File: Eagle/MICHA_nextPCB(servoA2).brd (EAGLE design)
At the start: 110.5 x 83.1 mm, 71 parts, among them IC1 LM4041A12LP, K1 PIN20X2, T1 BSS84, U1 ARDUINO_MKR_ZERO, U2 MIKROE_CLICK_UPGRADE, U3 MAX4528CSA, X1 SS-7188S-A-NF_V2, X2 SS-7188S-A-NF_V2, X3 SS-7188S-A-NF_V2, X4 SS-7188S-A-NF_V2, X5 SS-7188S-A-NF_V2, X6 SS-7188S-A-NF_V2, X7 BUCHANAN_4_3.5MM, X8 MPT_0,5/_2-2,54_1725656_2

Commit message: Btn & thermis zener replaced by Schottky
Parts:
- removed Z10, Z4, Z5, Z6, Z7, Z8, Z9: 3,3V, Zener_SMA:ZENER_SMA
- added DS1, DS2, DS3, DS4: SDM10M45SD, SchottkyDiodes_SDM10M45SD:SDM10M45SD_SOT-26
- moved R21 3.17 mm to (21.0, -0.64)
- moved R14 2.22 mm to (19.4, 8.57)
- moved R15 2.22 mm to (22.5, 8.57)
- moved R16 2.22 mm to (25.7, 8.57)
- moved R13 0.95 mm to (16.2, 8.57)
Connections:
- net GND: now also DS1.1, DS1.4, DS2.1, DS2.4, DS3.1, DS3.4, DS4.1, DS4.4; no longer Z10.A, Z4.A, Z5.A, Z6.A, Z7.A, Z8.A, Z9.A
- net N$11: now also DS1.3; no longer Z4.C
- net N$12: now also DS1.6; no longer Z5.C
- net N$13: now also DS2.3; no longer Z6.C
- net N$14: now also DS2.6; no longer Z7.C
- net PI_STOP_BTN: now also DS4.3; no longer Z10.C
- net PUMP_PAUSE_BTN: now also DS3.6; no longer Z8.C
- net PUMP_START_BTN: now also DS3.3; no longer Z9.C
- net VDD: now also DS1.2, DS1.5, DS2.2, DS2.5, DS3.2, DS3.5, DS4.2, DS4.5
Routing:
- net VDD: track 51.5 -> 168.6 mm, vias 1 -> 9
- net N$11: track 85.0 -> 75.9 mm
- net N$14: track 63.4 -> 72.3 mm
- net N$13: track 74.8 -> 69.6 mm
- net N$6: track 87.4 -> 84.7 mm
- net N$12: track 72.6 -> 74.6 mm
- net GND: track 8.64 -> 10.6 mm, vias 4 -> 6
- net THERMI2: track 6.82 -> 5.51 mm
- net PUMP_START_BTN: track 66.3 -> 65.4 mm

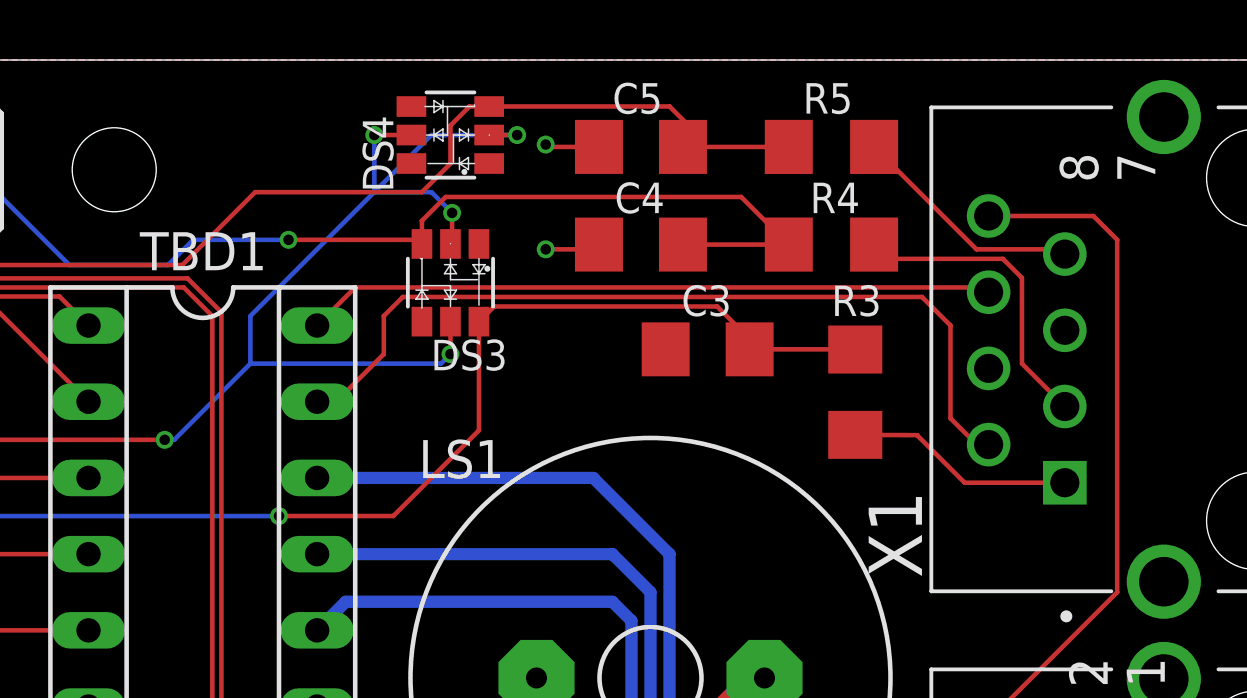
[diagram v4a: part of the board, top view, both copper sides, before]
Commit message: Button diodes between resistor and capacitor
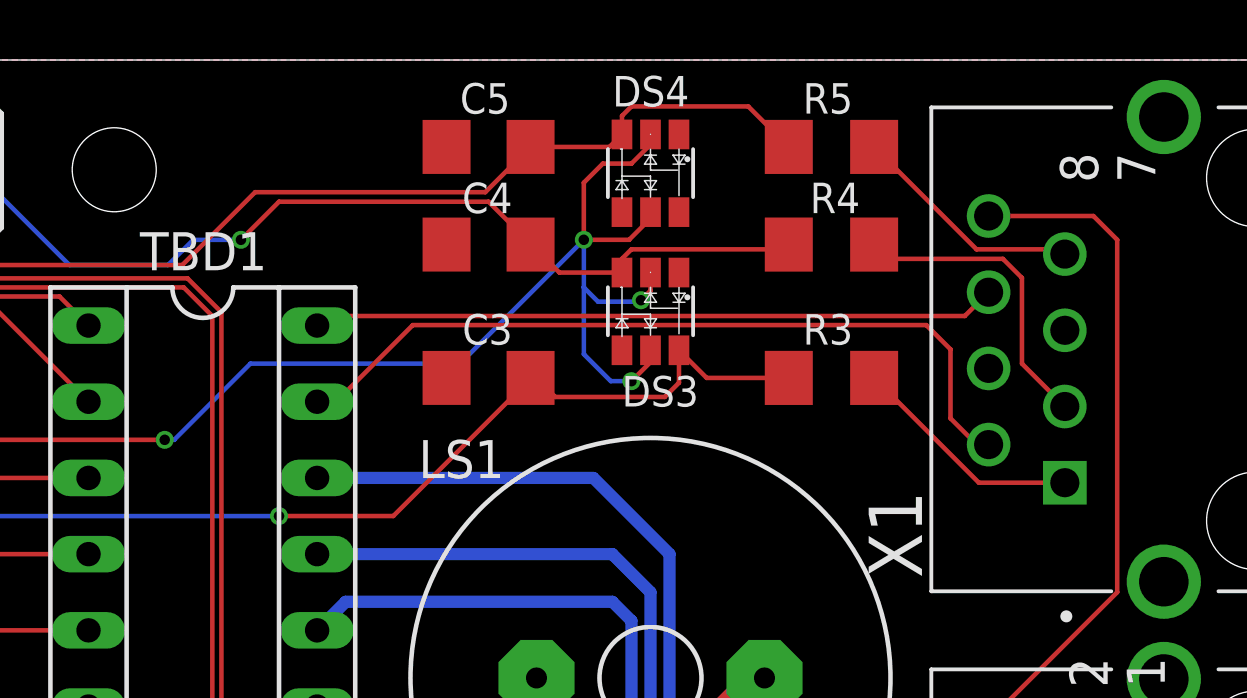
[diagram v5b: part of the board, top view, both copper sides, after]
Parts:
- moved C3 7.36 mm to (74.0, 45.6)
- moved DS4 6.79 mm to (79.4, 52.4), turned to 180 degrees
- moved DS3 6.74 mm to (79.4, 47.8)
- moved C4 5.08 mm to (74.0, 50.0)
- moved C5 5.08 mm to (74.0, 53.3)
- moved R3 0.93 mm to (85.4, 45.6), turned to 0 degrees
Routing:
- net PUMP_PAUSE_BTN: track 72.8 -> 68.6 mm
- net GND: track 10.6 -> 6.98 mm, vias 6 -> 4
- net PUMP_START_BTN: track 65.4 -> 62.3 mm
- net PUMP_PAUSE_LED: track 28.4 -> 26.4 mm
- net VDD: track 168.6 -> 170.5 mm, vias 9 -> 8
- net PI_STOP_BTN: track 40.0 -> 39.1 mm

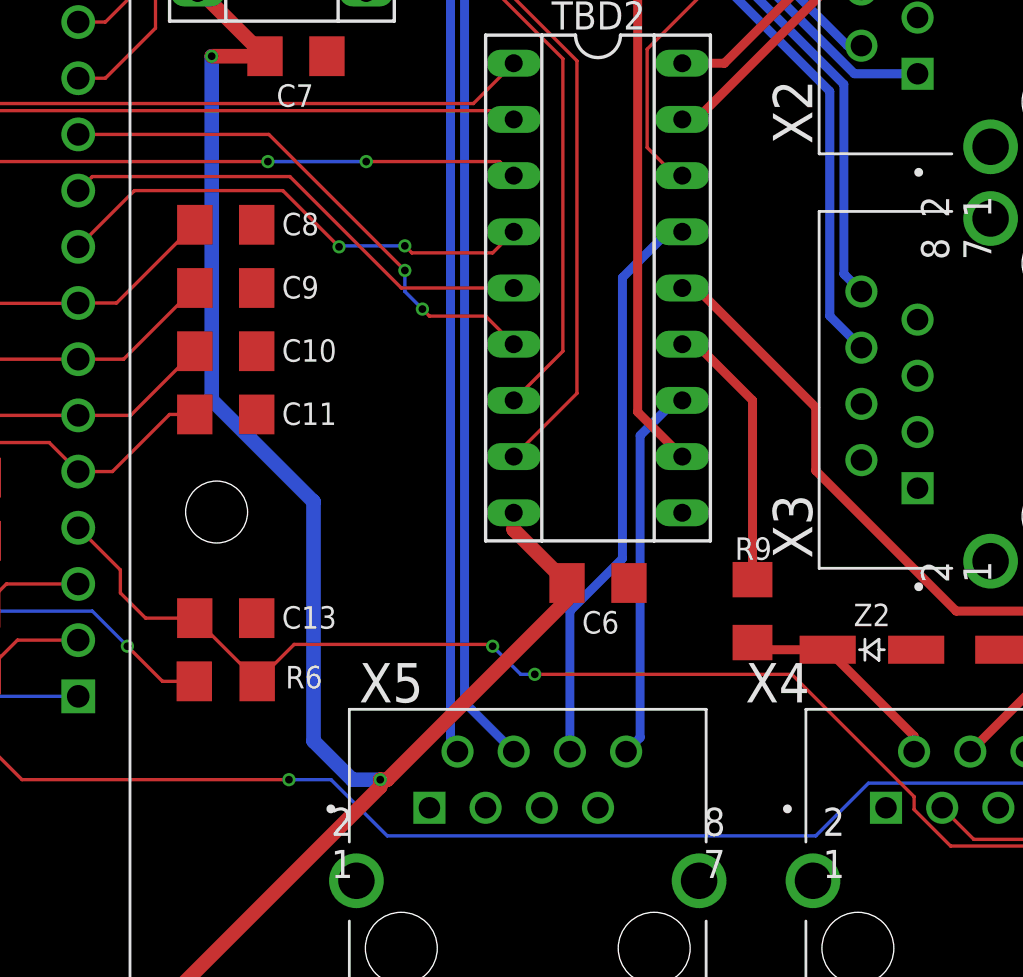
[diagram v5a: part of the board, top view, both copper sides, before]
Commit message: add jumpers for reserve and pump_relay
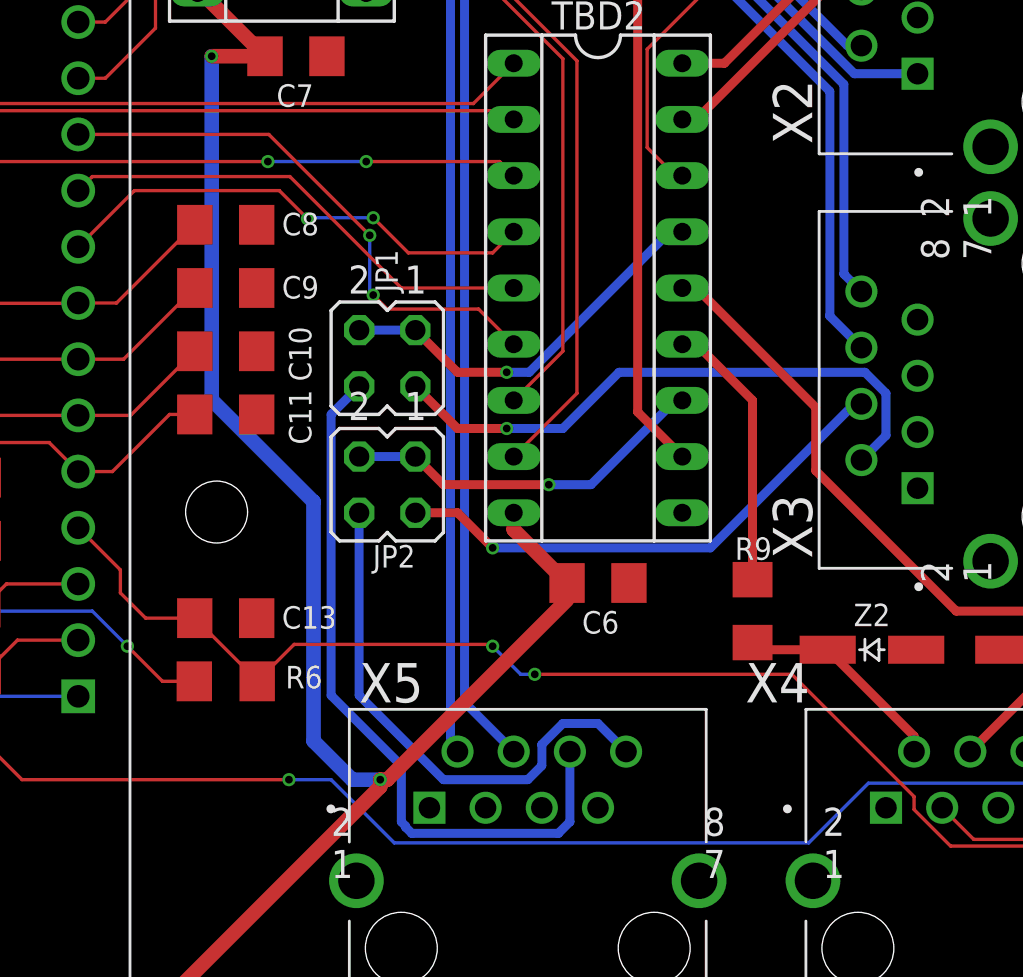
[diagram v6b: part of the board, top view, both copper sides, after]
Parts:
- added JP1, JP2: (no value), jumper:JP2Q
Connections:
- new net N$19: JP1.4, X5.6
- new net N$20: JP1.2, X3.2
- new net N$21: JP2.4, X5.8
- new net N$22: JP2.2, X3.4
- net PUMP_RELAY: now also JP1.1, JP1.3; no longer X5.6
- net RESERVE: now also JP2.1, JP2.3; no longer X5.8
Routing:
- net N$19: track 0.00 -> 32.8 mm
- net N$20: track 0.00 -> 27.0 mm, vias 0 -> 1
- net N$21: track 0.00 -> 24.0 mm
- net N$22: track 0.00 -> 23.5 mm, vias 0 -> 1
- net PUMP_RELAY: track 26.0 -> 18.0 mm, vias 0 -> 1
- net D2: track 24.2 -> 25.2 mm
- net RESERVE: track 17.1 -> 16.7 mm, vias 0 -> 1

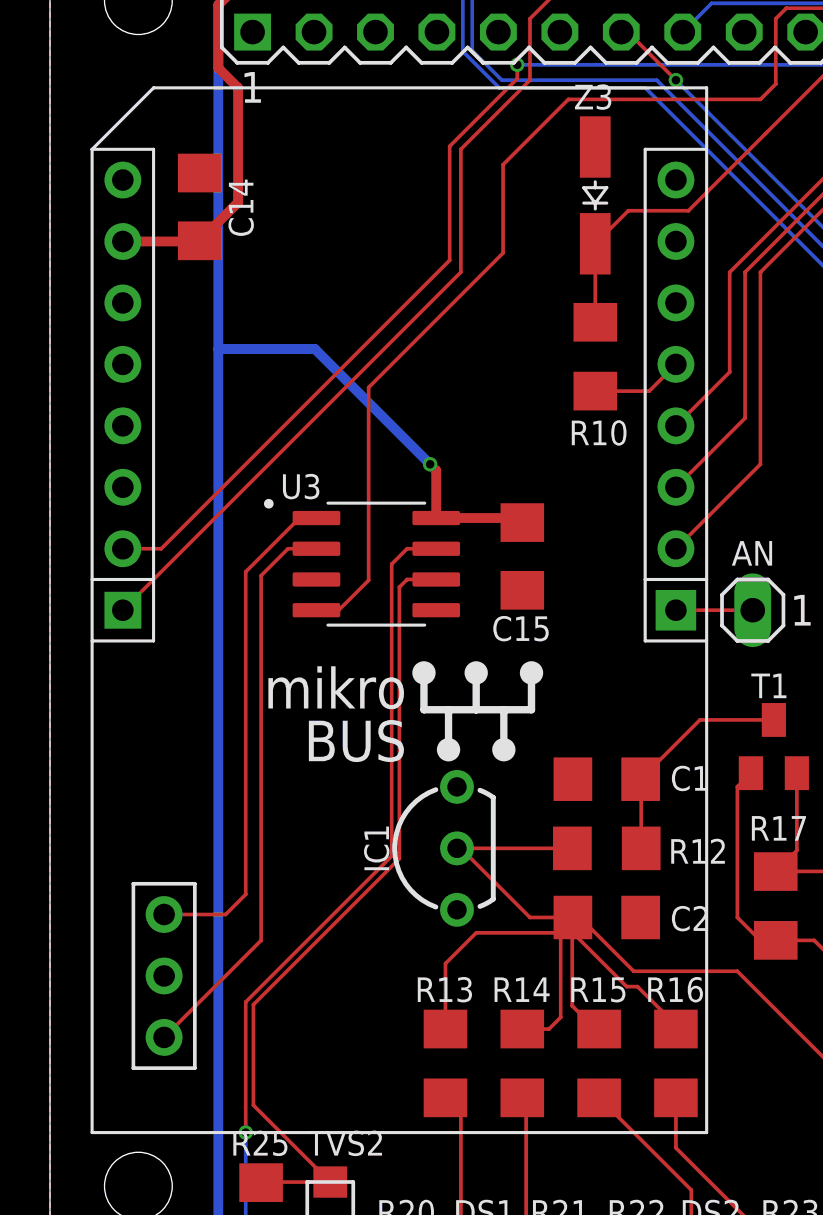
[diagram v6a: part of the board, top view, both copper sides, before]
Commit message: Mikrobus footprint updated
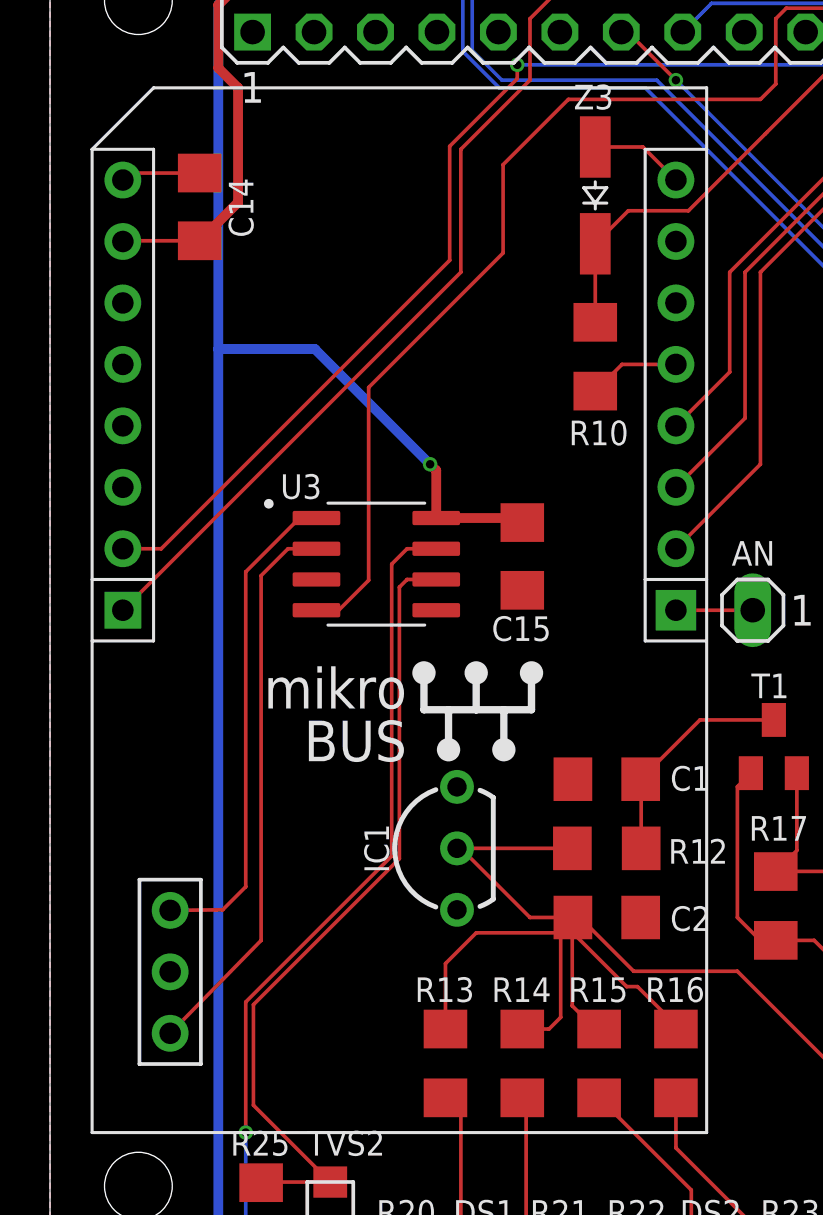
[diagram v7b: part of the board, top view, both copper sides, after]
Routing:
- net GND: track 6.98 -> 14.2 mm
- net N$10: track 20.9 -> 20.4 mm
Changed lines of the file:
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@@
 <contactref element="C13" pad="2"/>
 <contactref element="C14" pad="2"/>
-<contactref element="U2" pad="R_GND2"/>
-<contactref element="U2" pad="R_GND1"/>
 <contactref element="Z1" pad="A"/>
 <contactref element="Z2" pad="A"/>
@@
 <contactref element="DS4" pad="1"/>
 <contactref element="DS4" pad="4"/>
+<contactref element="U2" pad="R_GND1"/>
+<contactref element="U2" pad="R_GND2"/>
+<wire x1="25.7175" y1="45.085" x2="24.3525" y2="46.45" width="0.1524" layer="1"/>
+<wire x1="24.3525" y1="46.45" x2="22.38375" y2="46.45" width="0.1524" layer="1"/>
+<wire x1="2.8575" y1="45.085" x2="3.14625" y2="45.37375" width="0.1524" layer="1"/>
+<wire x1="3.14625" y1="45.37375" x2="6.0325" y2="45.37375" width="0.1524" layer="1"/>
 </signal>
 <signal name="5V">
@@
 <wire x1="15.5575" y1="33.3375" x2="10.795" y2="38.1" width="0.4064" layer="16"/>
 <wire x1="10.795" y1="38.1" x2="6.8032" y2="38.1" width="0.4064" layer="16"/>
+<contactref element="C14" pad="1"/>
+<wire x1="6.0325" y1="42.57375" x2="7.62" y2="44.16125" width="0.4064" layer="1"/>
 <contactref element="U2" pad="R_5V"/>
-<contactref element="C14" pad="1"/>
-<wire x1="6.0325" y1="42.57375" x2="6.00375" y2="42.545" width="0.4064" layer="1"/>
-<wire x1="6.00375" y1="42.545" x2="2.8575" y2="42.545" width="0.4064" layer="1"/>
-<wire x1="6.0325" y1="42.57375" x2="7.62" y2="44.16125" width="0.4064" layer="1"/>
+<wire x1="2.8575" y1="42.545" x2="2.88625" y2="42.57375" width="0.1524" layer="1"/>
+<wire x1="2.88625" y1="42.57375" x2="6.0325" y2="42.57375" width="0.1524" layer="1"/>
 </signal>
 <signal name="PUMP_PAUSE_BTN">
@@
 </signal>
 <signal name="N$1">
-<contactref element="U2" pad="B"/>
 <contactref element="U3" pad="2"/>
-<wire x1="4.563309375" y1="9.64806875" x2="8.5725" y2="13.657259375" width="0.1524" layer="1"/>
-<wire x1="8.5725" y1="13.657259375" x2="8.5725" y2="28.73375" width="0.1524" layer="1"/>
+<wire x1="8.5725" y1="28.73375" x2="8.5725" y2="13.657259375" width="0.1524" layer="1"/>
 <wire x1="8.5725" y1="28.73375" x2="9.68375" y2="29.845" width="0.1524" layer="1"/>
 <wire x1="9.68375" y1="29.845" x2="10.86" y2="29.845" width="0.1524" layer="1"/>
+<contactref element="U2" pad="B"/>
+<wire x1="8.5725" y1="13.657259375" x2="4.813309375" y2="9.81806875" width="0.1524" layer="1"/>
 </signal>
 <signal name="N$10">
-<contactref element="U2" pad="A"/>
 <contactref element="U3" pad="1"/>
-<wire x1="4.563309375" y1="14.72806875" x2="7.10806875" y2="14.72806875" width="0.1524" layer="1"/>
-<wire x1="7.9375" y1="15.5575" x2="7.9375" y2="28.8925" width="0.1524" layer="1"/>
+<wire x1="7.9375" y1="28.8925" x2="7.9375" y2="15.875" width="0.1524" layer="1"/>
 <wire x1="7.9375" y1="28.8925" x2="10.16" y2="31.115" width="0.1524" layer="1"/>
 <wire x1="10.16" y1="31.115" x2="10.86" y2="31.115" width="0.1524" layer="1"/>
-<wire x1="7.10806875" y1="14.72806875" x2="7.9375" y2="15.5575" width="0.1524" layer="1"/>
+<contactref element="U2" pad="A"/>
+<wire x1="7.9375" y1="15.875" x2="6.985" y2="14.9225" width="0.1524" layer="1"/>
+<wire x1="6.985" y1="14.9225" x2="4.813309375" y2="14.89806875" width="0.1524" layer="1"/>
 </signal>
 <signal name="R_X">
@@
 <wire x1="28.2575" y1="-1.9325" x2="28.255" y2="-1.935" width="0.1524" layer="1"/>
 </signal>
-<signal name="N$15">
-<contactref element="U2" pad="R_MISO"/>
-<contactref element="R10" pad="2"/>
-<wire x1="22.38375" y1="36.3605" x2="24.613" y2="36.3605" width="0.1524" layer="1"/>
-<wire x1="24.613" y1="36.3605" x2="25.7175" y2="37.465" width="0.1524" layer="1"/>
-</signal>
-<signal name="N$16">
-<contactref element="U2" pad="R_AN"/>
-<contactref element="AN" pad="1"/>
-<wire x1="25.7175" y1="27.305" x2="28.8925" y2="27.305" width="0.1524" layer="1"/>
-</signal>
 <signal name="N$17">
 <contactref element="X8" pad="2"/>
@@
 <wire x1="72.39" y1="3.4925" x2="70.485" y2="3.4925" width="0.4064" layer="1"/>
 </signal>
+<signal name="N$16">
+<contactref element="U2" pad="R_AN"/>
+<contactref element="AN" pad="1"/>
+<wire x1="25.7175" y1="27.305" x2="28.8925" y2="27.305" width="0.1524" layer="1"/>
+</signal>
+<signal name="N$15">
+<contactref element="U2" pad="R_MISO"/>
+<contactref element="R10" pad="2"/>
+<wire x1="22.38375" y1="36.3605" x2="23.48825" y2="37.465" width="0.1524" layer="1"/>
+<wire x1="23.48825" y1="37.465" x2="25.7175" y2="37.465" width="0.1524" layer="1"/>
+</signal>
 </signals>
